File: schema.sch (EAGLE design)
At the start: 24 parts, among them IC1 IPS6404L-SQ-SPN, IC3 HT7333, J1 FH12-24S-0.5SH(55), J3 C10418, U1 ESP-32S, U3 CH340ESMD

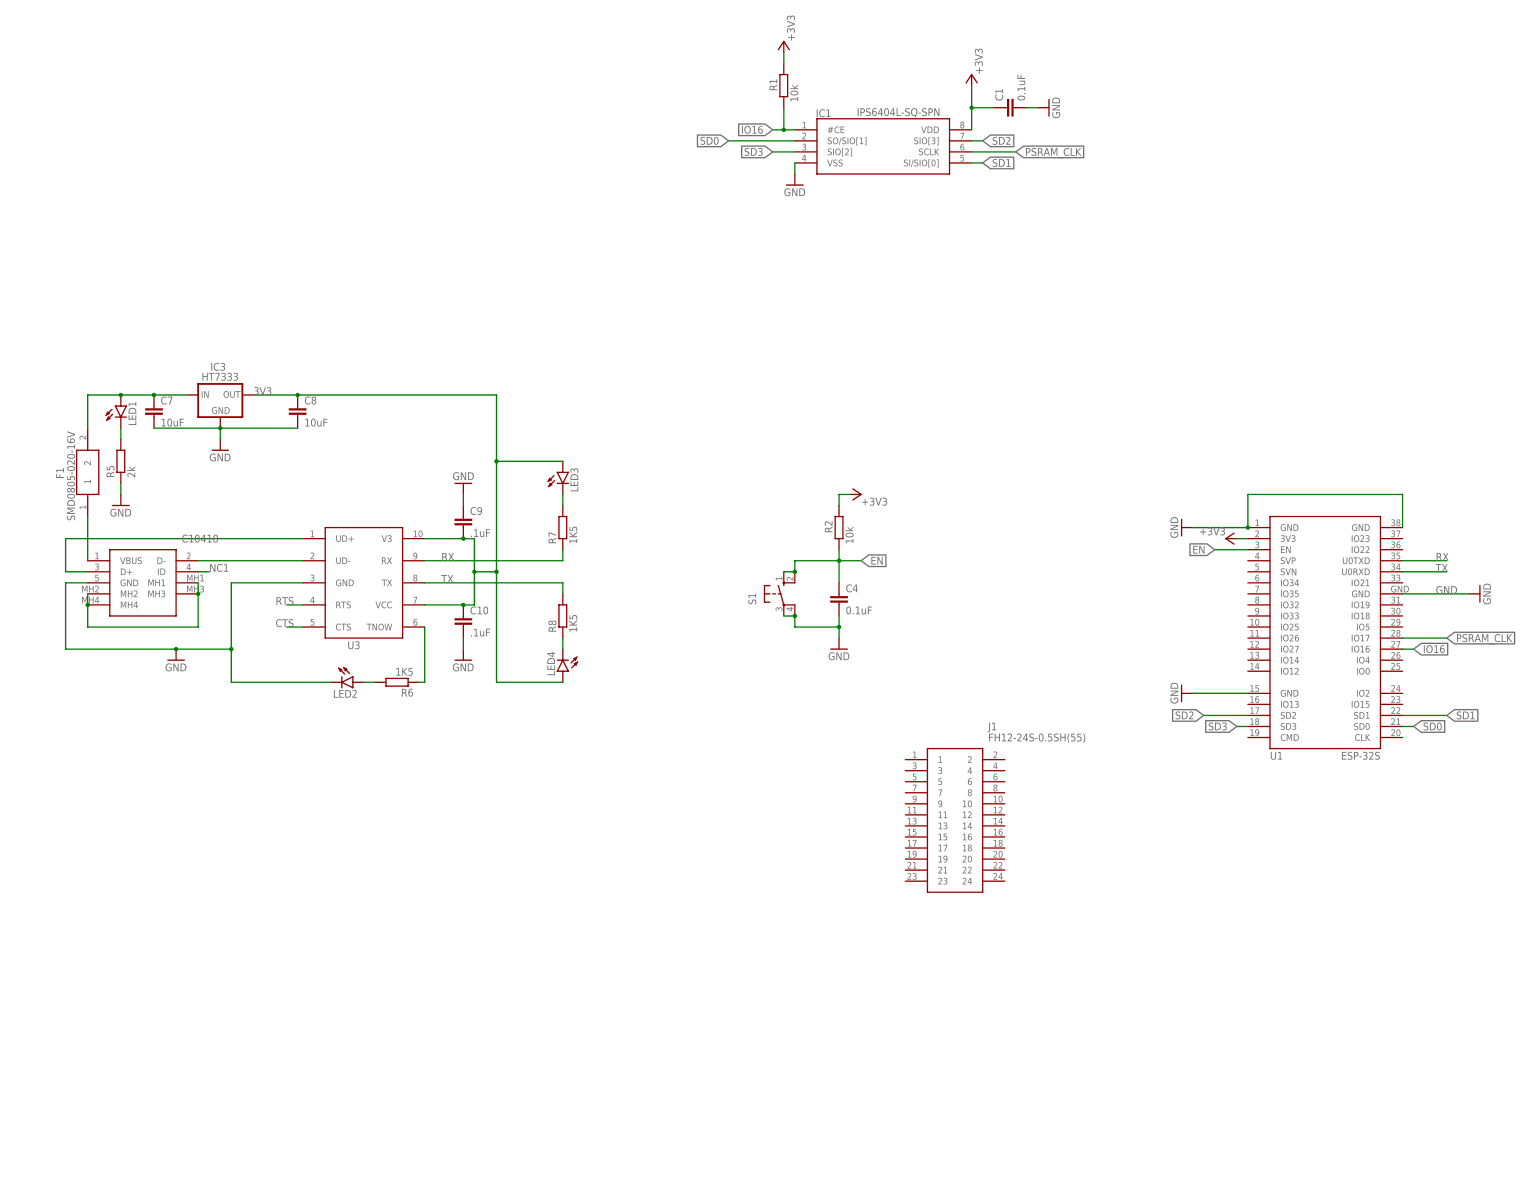
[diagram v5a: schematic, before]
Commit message: CAM ribbon connection
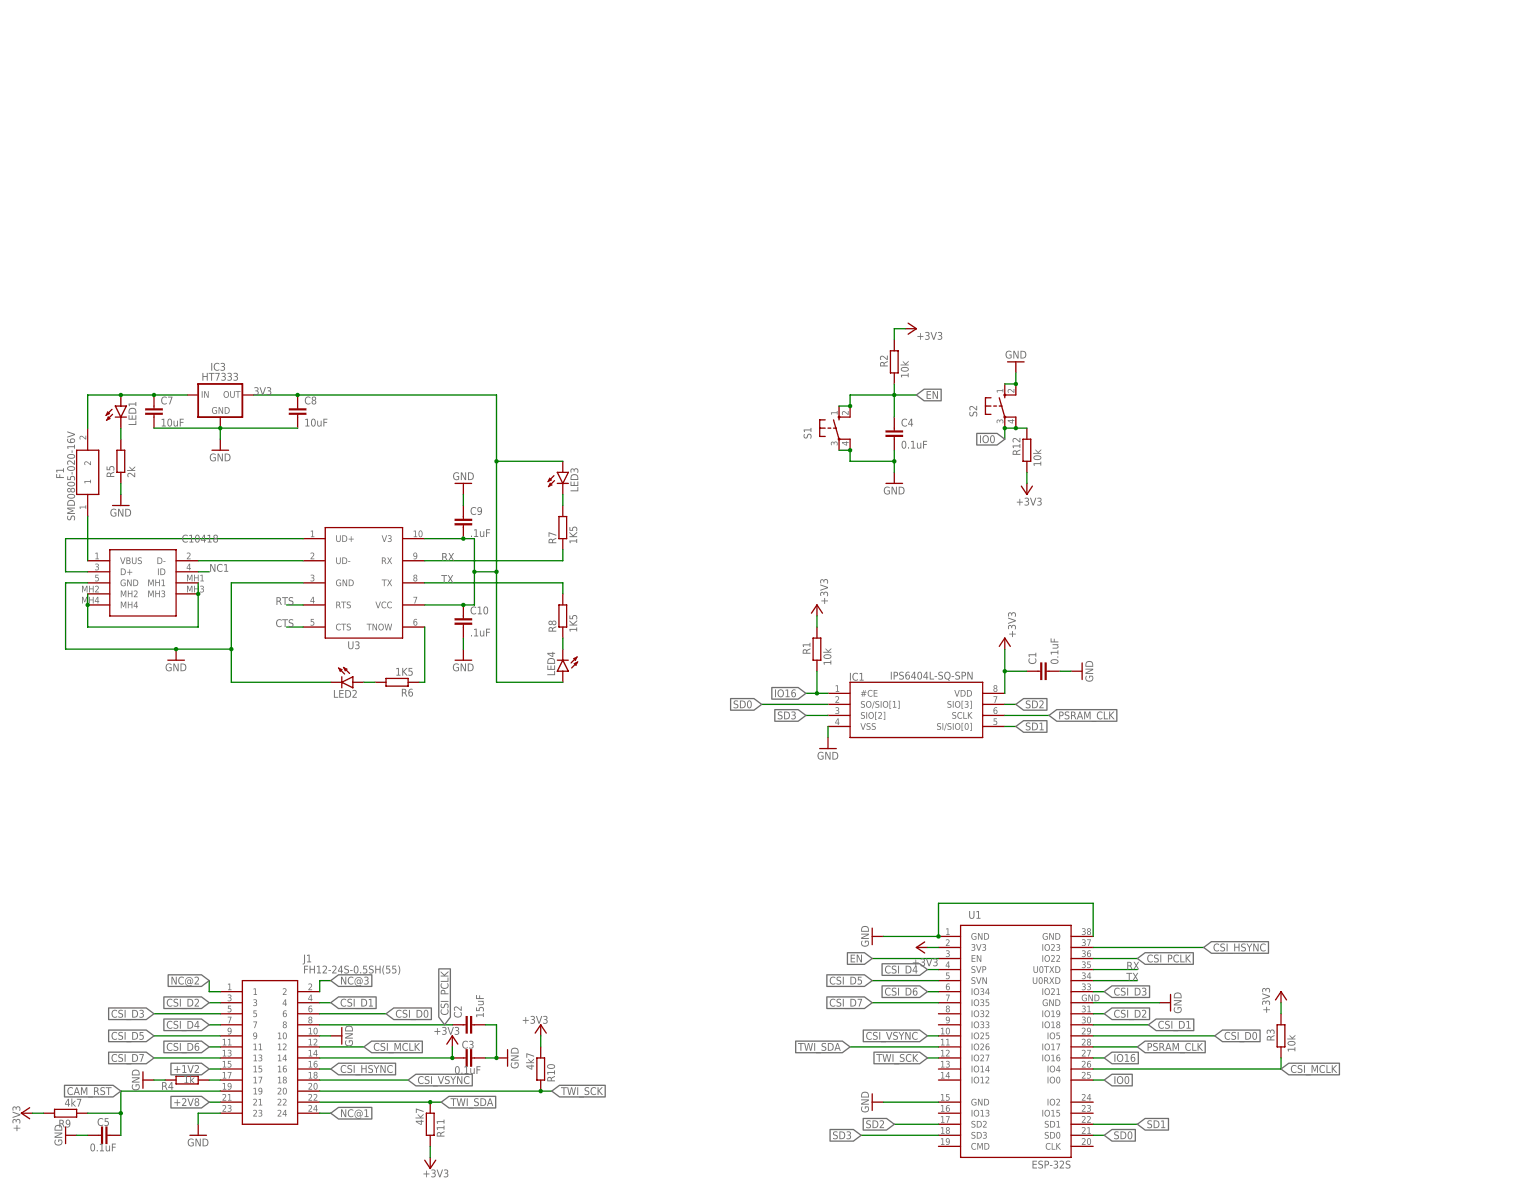
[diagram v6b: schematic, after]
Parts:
- added C2: 15uF, rcl:C-EUC0805
- added C3, C5: 0.1uF, rcl:C-EUC0805
- added R10, R11, R9: 4k7, rcl:R-EU_R0805
- added R12, R3: 10k, rcl:R-EU_R0805
- added R4: 1k, rcl:R-EU_R0805
- added S2: (no value), switch-omron:10-XX
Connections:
- new net +1V2: J1.15
- new net +2V8: J1.21
- new net CAM_RST: C5.2, J1.19, R9.1
- new net CSI_D0: J1.6, U1.IO5
- new net CSI_D1: J1.4, U1.IO18
- new net CSI_D2: J1.3, U1.IO19
- new net CSI_D3: J1.5, U1.IO21
- new net CSI_D4: J1.7, U1.SVP
- new net CSI_D5: J1.9, U1.SVN
- new net CSI_D6: J1.11, U1.IO34
- new net CSI_D7: J1.13, U1.IO35
- new net CSI_HSYNC: J1.16, U1.IO23
- new net CSI_MCLK: J1.12, R3.1, U1.IO4
- new net CSI_PCLK: C2.1, J1.8, U1.IO22
- new net CSI_VSYNC: J1.18, U1.IO25
- new net IO0: R12.2, S2.P, S2.P1, U1.IO0
- new net N$1: J1.17, R4.1
- new net NC@1: J1.24
- new net NC@2: J1.1
- new net NC@3: J1.2
- new net TWI_SCK: J1.20, R10.2, U1.IO27
- new net TWI_SDA: J1.22, R11.1, U1.IO26
- net +3V3: now also C3.1, J1.14, R10.1, R11.2, R12.1, R3.2, R9.2
- net GND: now also C2.2, C3.2, C5.1, J1.10, J1.23, R4.2, S2.S, S2.S1
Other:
- moved on the sheet: C1, C4, IC1, J1, R1, R2, S1, U1
